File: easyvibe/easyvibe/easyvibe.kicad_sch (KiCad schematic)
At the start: 85 parts, among them SW1 SW_DPDT_x2, U1 TL062, U2 TL062, U3 TL062, U4 TL062

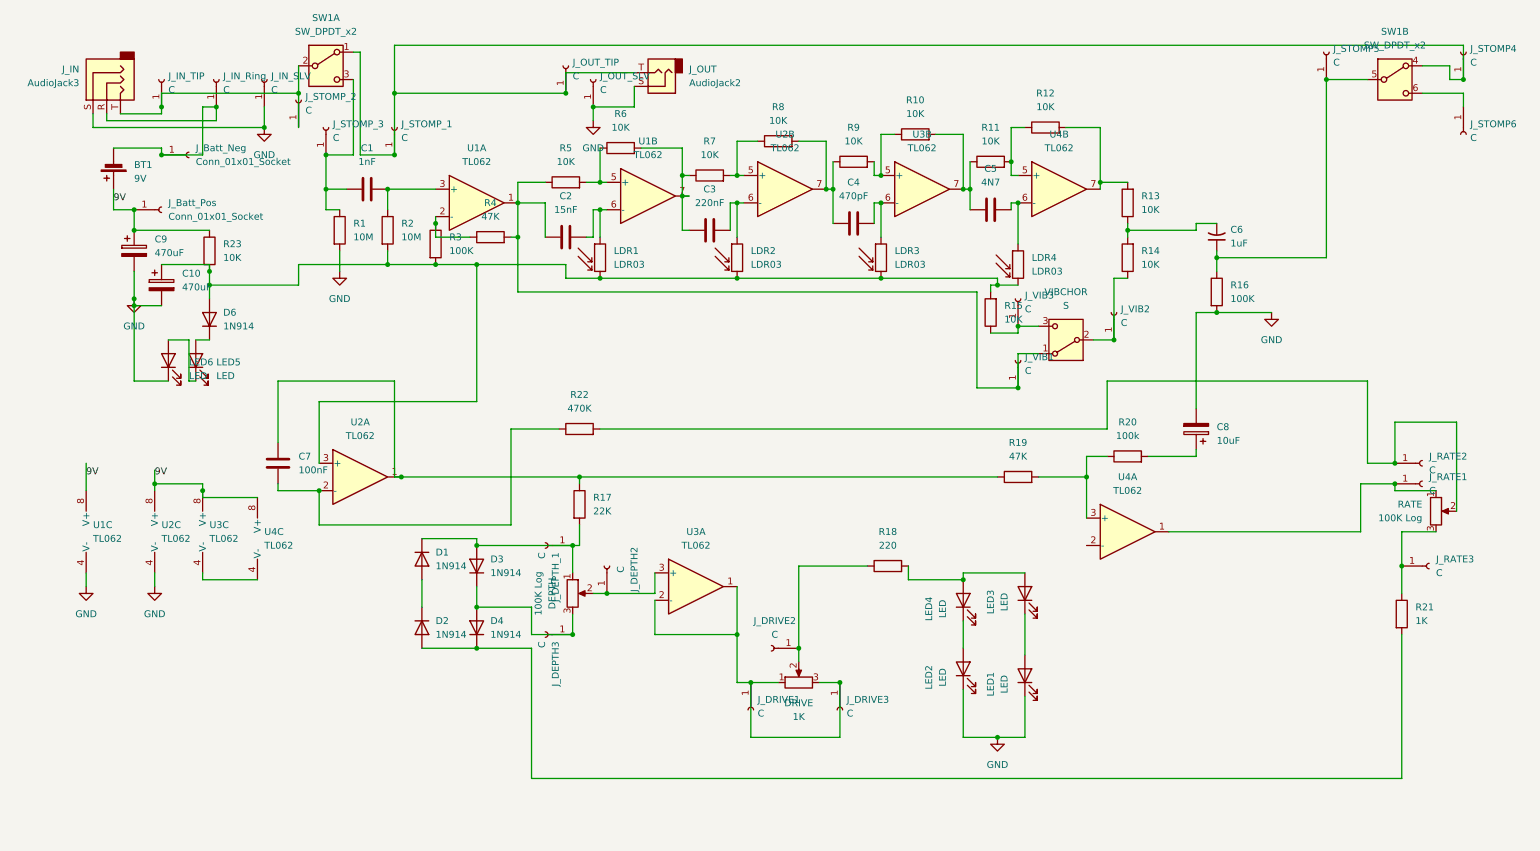
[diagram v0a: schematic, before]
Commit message: got import from digikey models working
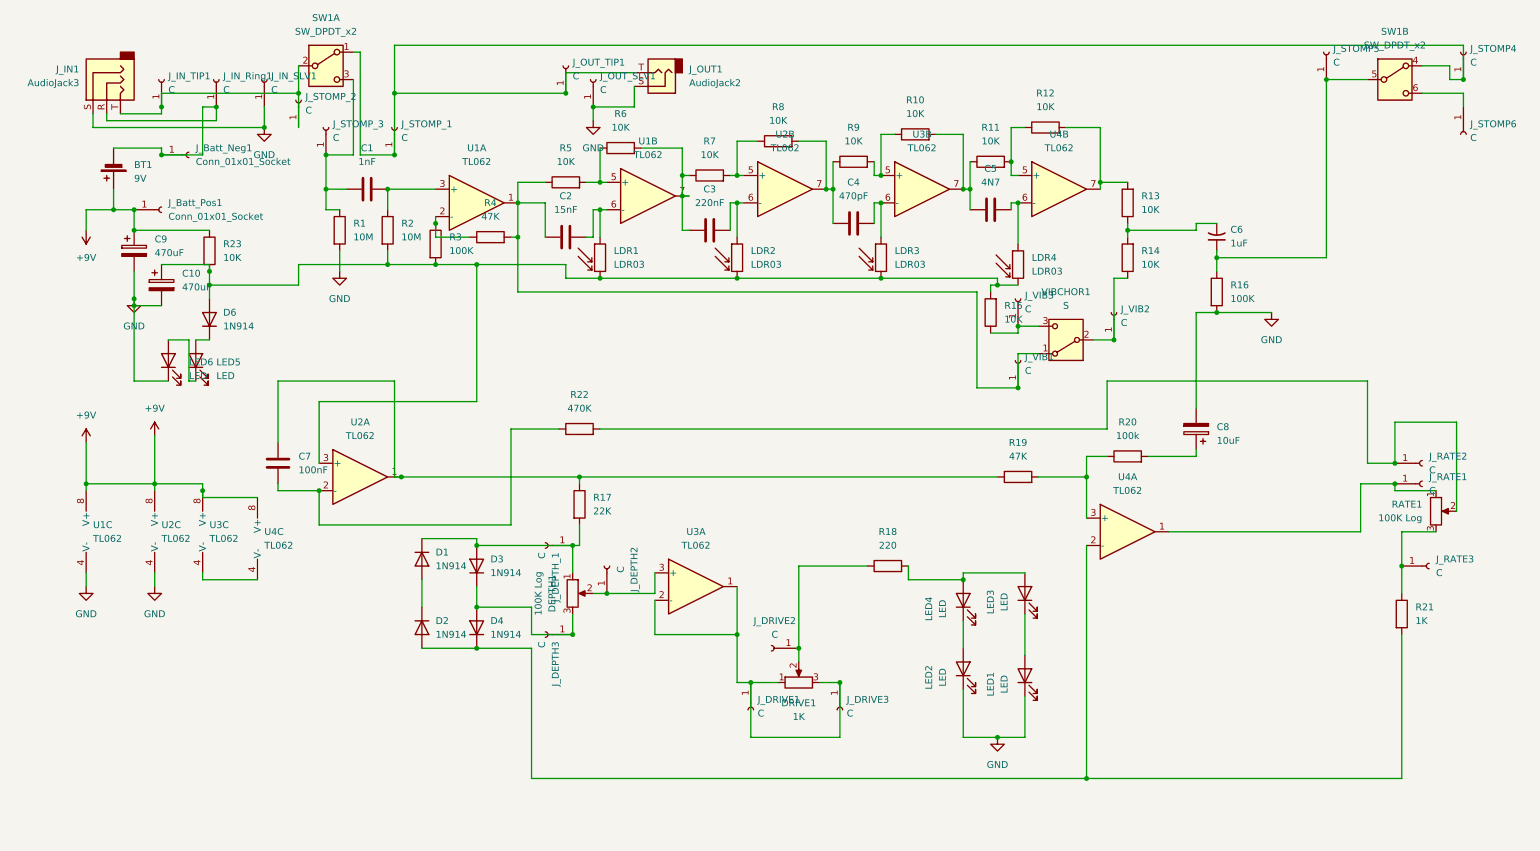
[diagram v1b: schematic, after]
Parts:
- R10, R11, R12, R13, R14, R15, R23, R5, R6, R7, R8, R9: footprint (none) -> Snapeda:YAG_MF25_YAG
- renumbered DEPTH to DEPTH1, DRIVE to DRIVE1, J_Batt_Neg to J_Batt_Neg1, J_Batt_Pos to J_Batt_Pos1, J_IN to J_IN1, J_IN_Ring to J_IN_Ring1, J_IN_SLV to J_IN_SLV1, J_IN_TIP to J_IN_TIP1, J_OUT to J_OUT1, J_OUT_SLV to J_OUT_SLV1, J_OUT_TIP to J_OUT_TIP1, RATE to RATE1, VIBCHOR to VIBCHOR1
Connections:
- net at D2.2 (A), D4.1 (K), R21.2: now also U4.2 (-)
- net 9V renamed +9V

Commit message: all footprints
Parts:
- C1, C2, C3, C5, C7: footprint (none) -> Capacitor_THT:C_Rect_L7.2mm_W2.5mm_P5.00mm_FKS2_FKP2_MKS2_MKP2
- C10, C9: footprint (none) -> Capacitor_THT:CP_Radial_D8.0mm_P3.50mm
- C4: footprint (none) -> Capacitor_THT:C_Rect_L7.2mm_W4.5mm_P5.00mm_FKS2_FKP2_MKS2_MKP2
- C6: footprint (none) -> Capacitor_THT:C_Radial_D5.0mm_H5.0mm_P2.00mm
- C8: footprint (none) -> Capacitor_THT:CP_Radial_D5.0mm_P2.00mm
- D1, D2, D3, D4, D6: footprint (none) -> Snapeda:AFL-W2C8.9D
- DRIVE1: footprint (none) -> Potentiometer_THT:Potentiometer_Runtron_RM-063_Horizontal
- J_Batt_Neg1, J_Batt_Pos1, J_DEPTH2, J_DEPTH3, J_DEPTH_1, J_DRIVE1, J_DRIVE2, J_DRIVE3, J_IN_Ring1, J_IN_SLV1, J_IN_TIP1, J_OUT_SLV1, J_OUT_TIP1, J_RATE1, J_RATE2, J_RATE3, J_STOMP4, J_STOMP5, J_STOMP6, J_STOMP_1, J_STOMP_2, J_STOMP_3, J_VIB1, J_VIB2, J_VIB3: footprint (none) -> Connector_PinSocket_2.54mm:PinSocket_1x01_P2.54mm_Vertical
- LED1, LED2, LED3, LED4, LED5, LED6: footprint (none) -> Snapeda:T-100_4P8X3P15_ONS
- R1, R2: footprint (none) -> Resistor_THT:R_Axial_DIN0207_L6.3mm_D2.5mm_P7.62mm_Horizontal
- R16, R17, R18, R19, R20, R21, R22, R3, R4: footprint (none) -> Snapeda:RES_LR1_TYCO_TYC
- U1, U2, U3, U4: footprint (none) -> Package_DIP:DIP-8_W7.62mm

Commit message: Added board cuts and mounting holes
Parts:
- added H1, H2, H3, H4: MountingHole, MountingHole:MountingHole_3.2mm_M3, symbol Mechanical:MountingHole

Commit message: initial component placement everywheres
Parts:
- removed J_DRIVE1, J_DRIVE2, J_DRIVE3: C, Connector_PinSocket_2.54mm:PinSocket_1x01_P2.54mm_Vertical, symbol Connector:Conn_01x01_Socket
- added R24: 1K, Snapeda:RES_LR1_TYCO_TYC, symbol Device:R
- LDR1, LDR2, LDR3, LDR4: footprint OptoDevice:R_LDR_10x8.5mm_P7.6mm_Vertical -> Snapeda:TO_NSL_19M_ADP
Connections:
- net at DEPTH1.2, J_DEPTH2.1 (Pin_1): now also R24.1; no longer U3.3 (+)
- new net: R24.2, U3.3 (+)

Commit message: some fixes
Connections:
- net at C8.1, R20.2: now also J_RATE1.1 (Pin_1), RATE1.1, U4.1
- net at R7.2, R8.1: now also U2.6 (-); no longer U2.5 (+)
- net at C3.2, LDR2.1: now also U2.5 (+); no longer U2.6 (-)
- net at J_STOMP5.1 (Pin_1), R16.1, SW1.5 (B): now also C6.2; no longer C6.1
- net at R13.1, R14.2: now also C6.1; no longer C6.2
- net at R5.2, R6.1: now also U1.6 (-); no longer U1.5 (+)
- net at C2.2, LDR1.1: now also U1.5 (+); no longer U1.6 (-)
- net at C5.2, LDR4.1: now also U4.5 (+); no longer U4.6 (-)
- net at R10.1, R9.2: now also U3.6 (-); no longer U3.5 (+)
- net at C4.2, LDR3.1: now also U3.5 (+); no longer U3.6 (-)
- net at R11.2, R12.1: now also U4.6 (-); no longer U4.5 (+)
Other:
- moved on the sheet: C6
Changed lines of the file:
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@@
 	)
 	(junction
-		(at 38.1 95.25)
+		(at 179.07 39.37)
 		(diameter 0)
 		(color 0 0 0 0)
 	)
 	(junction
-		(at 189.23 41.91)
+		(at 38.1 95.25)
 		(diameter 0)
 		(color 0 0 0 0)
@@
 	)
 	(junction
-		(at 259.08 90.17)
+		(at 163.83 36.83)
 		(diameter 0)
 		(color 0 0 0 0)
 	)
 	(junction
-		(at 137.16 55.88)
+		(at 259.08 90.17)
 		(diameter 0)
 		(color 0 0 0 0)
 	)
 	(junction
-		(at 189.23 76.2)
+		(at 137.16 55.88)
 		(diameter 0)
 		(color 0 0 0 0)
 	)
 	(junction
-		(at 88.9 105.41)
+		(at 189.23 76.2)
 		(diameter 0)
 		(color 0 0 0 0)
 	)
 	(junction
-		(at 111.76 43.18)
+		(at 88.9 105.41)
 		(diameter 0)
 		(color 0 0 0 0)
@@
 	)
 	(junction
+		(at 137.16 36.83)
+		(diameter 0)
+		(color 0 0 0 0)
+	)
+	(junction
 		(at 88.9 53.34)
 		(diameter 0)
@@
 	)
 	(junction
-		(at 107.95 92.71)
+		(at 218.44 102.87)
 		(diameter 0)
 		(color 0 0 0 0)
 	)
 	(junction
-		(at 163.83 36.83)
+		(at 107.95 92.71)
 		(diameter 0)
 		(color 0 0 0 0)
@@
 	)
 	(junction
-		(at 25.4 60.96)
+		(at 189.23 41.91)
 		(diameter 0)
 		(color 0 0 0 0)
 	)
 	(junction
-		(at 271.78 19.05)
+		(at 25.4 60.96)
 		(diameter 0)
 		(color 0 0 0 0)
 	)
 	(junction
-		(at 179.07 39.37)
+		(at 271.78 19.05)
 		(diameter 0)
 		(color 0 0 0 0)
@@
 	)
 	(junction
+		(at 111.76 43.18)
+		(diameter 0)
+		(color 0 0 0 0)
+	)
+	(junction
 		(at 25.4 46.99)
 		(diameter 0)
@@
 	)
 	(junction
-		(at 204.47 38.1)
+		(at 163.83 41.91)
 		(diameter 0)
 		(color 0 0 0 0)
@@
 	)
 	(junction
-		(at 137.16 41.91)
-		(diameter 0)
-		(color 0 0 0 0)
-	)
-	(junction
 		(at 21.59 43.18)
 		(diameter 0)
@@
 	)
 	(junction
-		(at 163.83 41.91)
+		(at 218.44 88.9)
 		(diameter 0)
 		(color 0 0 0 0)
@@
 	)
 	(junction
-		(at 226.06 62.23)
+		(at 111.76 38.1)
 		(diameter 0)
 		(color 0 0 0 0)
 	)
 	(junction
-		(at 137.16 36.83)
+		(at 226.06 62.23)
 		(diameter 0)
 		(color 0 0 0 0)
@@
 	)
 	(junction
-		(at 201.93 92.71)
+		(at 204.47 38.1)
 		(diameter 0)
 		(color 0 0 0 0)
 	)
 	(junction
-		(at 127 40.64)
+		(at 201.93 92.71)
 		(diameter 0)
 		(color 0 0 0 0)
 	)
 	(junction
-		(at 111.76 38.1)
+		(at 127 40.64)
 		(diameter 0)
 		(color 0 0 0 0)
@@
 	)
 	(junction
+		(at 137.16 41.91)
+		(diameter 0)
+		(color 0 0 0 0)
+	)
+	(junction
 		(at 153.67 39.37)
 		(diameter 0)
@@
 	(wire
 		(pts
-			(xy 217.17 102.87) (xy 252.73 102.87)
+			(xy 217.17 102.87) (xy 218.44 102.87)
 		)
 		(stroke
@@
 	(wire
 		(pts
+			(xy 218.44 102.87) (xy 252.73 102.87)
+		)
+		(stroke
+			(width 0)
+			(type default)
+		)
+	)
+	(wire
+		(pts
 			(xy 266.7 95.25) (xy 259.08 95.25)
 		)
@@
 	(wire
 		(pts
-			(xy 137.16 41.91) (xy 138.43 41.91)
+			(xy 55.88 16.51) (xy 55.88 21.59)
 		)
 		(stroke
@@
 	(wire
 		(pts
-			(xy 55.88 16.51) (xy 55.88 21.59)
+			(xy 270.51 99.06) (xy 270.51 82.55)
 		)
 		(stroke
@@
 	(wire
 		(pts
-			(xy 270.51 99.06) (xy 270.51 82.55)
+			(xy 25.4 74.93) (xy 25.4 60.96)
 		)
 		(stroke
@@
 	(wire
 		(pts
-			(xy 25.4 74.93) (xy 25.4 60.96)
+			(xy 111.76 83.82) (xy 205.74 83.82)
 		)
 		(stroke
@@
 	(wire
 		(pts
-			(xy 111.76 83.82) (xy 205.74 83.82)
+			(xy 119.38 31.75) (xy 127 31.75)
 		)
 		(stroke
@@
 	(wire
 		(pts
-			(xy 119.38 31.75) (xy 127 31.75)
+			(xy 269.24 16.51) (xy 269.24 19.05)
 		)
 		(stroke
@@
 	(wire
 		(pts
-			(xy 269.24 16.51) (xy 269.24 19.05)
+			(xy 88.9 124.46) (xy 99.06 124.46)
 		)
 		(stroke
@@
 	(wire
 		(pts
-			(xy 88.9 124.46) (xy 99.06 124.46)
+			(xy 137.16 36.83) (xy 138.43 36.83)
 		)
 		(stroke
@@
 	(wire
 		(pts
-			(xy 137.16 36.83) (xy 138.43 36.83)
+			(xy 187.96 34.29) (xy 187.96 36.83)
 		)
 		(stroke
@@
 	(wire
 		(pts
-			(xy 187.96 34.29) (xy 187.96 36.83)
+			(xy 218.44 88.9) (xy 213.36 88.9)
 		)
 		(stroke
@@
 	(wire
 		(pts
+			(xy 111.76 38.1) (xy 113.03 38.1)
+		)
+		(stroke
+			(width 0)
+			(type default)
+		)
+	)
+	(wire
+		(pts
 			(xy 189.23 41.91) (xy 189.23 49.53)
 		)
@@
 	(wire
 		(pts
+			(xy 218.44 88.9) (xy 218.44 102.87)
+		)
+		(stroke
+			(width 0)
+			(type default)
+		)
+	)
+	(wire
+		(pts
 			(xy 127 46.99) (xy 128.27 46.99)
 		)
@@
 	(wire
 		(pts
+			(xy 137.16 41.91) (xy 138.43 41.91)
+		)
+		(stroke
+			(width 0)
+			(type default)
+		)
+	)
+	(wire
+		(pts
 			(xy 139.7 140.97) (xy 156.21 140.97)
 		)
@@
 	(wire
 		(pts
-			(xy 111.76 43.18) (xy 113.03 43.18)
-		)
-		(stroke
-			(width 0)
-			(type default)
-		)
-	)
-	(wire
-		(pts
 			(xy 127 36.83) (xy 128.27 36.83)
 		)
@@
 	(wire
 		(pts
-			(xy 222.25 88.9) (xy 213.36 88.9)
+			(xy 222.25 88.9) (xy 218.44 88.9)
 		)
 		(stroke
@@
 	(wire
 		(pts
-			(xy 111.76 38.1) (xy 113.03 38.1)
-		)
-		(stroke
-			(width 0)
-			(type default)
-		)
-	)
-	(wire
-		(pts
 			(xy 111.76 31.75) (xy 111.76 38.1)
 		)
@@
 	(wire
 		(pts
+			(xy 111.76 43.18) (xy 113.03 43.18)
+		)
+		(stroke
+			(width 0)
+			(type default)
+		)
+	)
+	(wire
+		(pts
 			(xy 209.55 38.1) (xy 204.47 38.1)
 		)
@@
 		(lib_id "Amplifier_Operational:TL062")
 		(at 146.05 39.37 0)
+		(mirror x)
 		(unit 2)
 		(body_style 1)
@@
 		(in_pos_files yes)
 		(dnp no)
-		(fields_autoplaced yes)
 		(property "Reference" "U2"
-			(at 146.05 29.21 0)
+			(at 146.05 49.53 0)
 			(show_name no)
 			(do_not_autoplace no)
@@
 		)
 		(property "Value" "TL062"
-			(at 146.05 31.75 0)
+			(at 146.05 46.99 0)
 			(show_name no)
 			(do_not_autoplace no)
@@
 	(symbol
 		(lib_id "Device:C_Small_US")
-		(at 226.06 48.26 180)
+		(at 226.06 48.26 0)
+		(mirror y)
 		(unit 1)
 		(body_style 1)
@@
 		(in_pos_files yes)
 		(dnp no)
-		(fields_autoplaced yes)
 		(property "Reference" "C6"
-			(at 228.6 46.8629 0)
+			(at 228.6 49.6571 0)
 			(show_name no)
 			(do_not_autoplace no)
@@
 		)
 		(property "Value" "1uF"
-			(at 228.6 49.4029 0)
+			(at 228.6 47.1171 0)
 			(show_name no)
 			(do_not_autoplace no)
@@
 		(lib_id "Amplifier_Operational:TL062")
 		(at 120.65 40.64 0)
+		(mirror x)
 		(unit 2)
 		(body_style 1)
@@
 		(in_pos_files yes)
 		(dnp no)
-		(fields_autoplaced yes)
 		(property "Reference" "U1"
-			(at 120.65 30.48 0)
+			(at 120.65 50.8 0)
 			(show_name no)
 			(do_not_autoplace no)
@@
 		)
 		(property "Value" "TL062"
-			(at 120.65 33.02 0)
+			(at 120.65 48.26 0)
 			(show_name no)
 			(do_not_autoplace no)
@@
 		(lib_id "Amplifier_Operational:TL062")
 		(at 171.45 39.37 0)
+		(mirror x)
 		(unit 2)
 		(body_style 1)
@@
 		(in_pos_files yes)
 		(dnp no)
-		(fields_autoplaced yes)
 		(property "Reference" "U3"
-			(at 171.45 29.21 0)
+			(at 171.45 49.53 0)
 			(show_name no)
 			(do_not_autoplace no)
@@
 		)
 		(property "Value" "TL062"
-			(at 171.45 31.75 0)
+			(at 171.45 46.99 0)
 			(show_name no)
 			(do_not_autoplace no)
@@
 		(lib_id "Amplifier_Operational:TL062")
 		(at 196.85 39.37 0)
+		(mirror x)
 		(unit 2)
 		(body_style 1)
@@
 		(in_pos_files yes)
 		(dnp no)
-		(fields_autoplaced yes)
 		(property "Reference" "U4"
-			(at 196.85 29.21 0)
+			(at 196.85 49.53 0)
 			(show_name no)
 			(do_not_autoplace no)
@@
 		)
 		(property "Value" "TL062"
-			(at 196.85 31.75 0)
+			(at 196.85 46.99 0)
 			(show_name no)
 			(do_not_autoplace no)
@@
 		(in_pos_files yes)
 		(dnp no)
-		(fields_autoplaced yes)
 		(property "Reference" "U3"
 			(at 129.54 102.87 0)

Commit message: more tweaks, make board slightly smaller to fit box
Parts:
- removed R24: 1K, Snapeda:RES_LR1_TYCO_TYC, symbol Device:R
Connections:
- net at R21.2, U4.2 (-): now also C10.1, D2.1 (K), D4.2 (A), D6.2 (A), DEPTH1.3, J_DEPTH3.1 (Pin_1), LDR1.2, LDR2.2, LDR3.2, LDR4.2, R15.2, R2.2, R23.2, R3.2, U2.3 (+); no longer D2.2 (A), D4.1 (K)
- net at DEPTH1.1, J_DEPTH_1.1 (Pin_1), R17.2: now also D1.2 (A), D3.1 (K); no longer D1.1 (K), D3.2 (A)
- net at DEPTH1.2, J_DEPTH2.1 (Pin_1): now also U3.3 (+)
- new net: D3.2 (A), D4.1 (K)
- new net: D1.1 (K), D2.2 (A)
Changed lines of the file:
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@@
 	)
 	(junction
-		(at 106.68 121.92)
-		(diameter 0)
-		(color 0 0 0 0)
-	)
-	(junction
 		(at 179.07 111.76)
 		(diameter 0)
@@
 	)
 	(junction
+		(at 59.69 90.17)
+		(diameter 0)
+		(color 0 0 0 0)
+	)
+	(junction
 		(at 111.76 38.1)
 		(diameter 0)
@@
 	)
 	(junction
-		(at 204.47 38.1)
+		(at 78.74 124.46)
 		(diameter 0)
 		(color 0 0 0 0)
 	)
 	(junction
-		(at 201.93 92.71)
+		(at 106.68 121.92)
 		(diameter 0)
 		(color 0 0 0 0)
 	)
 	(junction
-		(at 127 40.64)
+		(at 204.47 38.1)
 		(diameter 0)
 		(color 0 0 0 0)
 	)
 	(junction
-		(at 88.9 116.84)
+		(at 201.93 92.71)
+		(diameter 0)
+		(color 0 0 0 0)
+	)
+	(junction
+		(at 127 40.64)
 		(diameter 0)
 		(color 0 0 0 0)
@@
 	)
 	(junction
+		(at 99.06 124.46)
+		(diameter 0)
+		(color 0 0 0 0)
+	)
+	(junction
 		(at 105.41 21.59)
 		(diameter 0)
@@
 	(wire
 		(pts
-			(xy 99.06 121.92) (xy 106.68 121.92)
-		)
-		(stroke
-			(width 0)
-			(type default)
-		)
-	)
-	(wire
-		(pts
 			(xy 201.93 148.59) (xy 260.35 148.59)
 		)
@@
 	(wire
 		(pts
+			(xy 59.69 90.17) (xy 57.15 90.17)
+		)
+		(stroke
+			(width 0)
+			(type default)
+		)
+	)
+	(wire
+		(pts
 			(xy 25.4 43.18) (xy 25.4 46.99)
 		)
@@
 	(wire
 		(pts
+			(xy 57.15 90.17) (xy 57.15 124.46)
+		)
+		(stroke
+			(width 0)
+			(type default)
+		)
+	)
+	(wire
+		(pts
 			(xy 63.5 50.8) (xy 63.5 54.61)
 		)
@@
 	(wire
 		(pts
+			(xy 106.68 124.46) (xy 99.06 124.46)
+		)
+		(stroke
+			(width 0)
+			(type default)
+		)
+	)
+	(wire
+		(pts
 			(xy 139.7 140.97) (xy 156.21 140.97)
 		)
@@
 	(wire
 		(pts
-			(xy 99.06 116.84) (xy 99.06 121.92)
-		)
-		(stroke
-			(width 0)
-			(type default)
-		)
-	)
-	(wire
-		(pts
 			(xy 16.51 43.18) (xy 16.51 46.99)
 		)
@@
 	(wire
 		(pts
+			(xy 114.3 111.76) (xy 121.92 111.76)
+		)
+		(stroke
+			(width 0)
+			(type default)
+		)
+	)
+	(wire
+		(pts
 			(xy 81.28 44.45) (xy 81.28 45.72)
 		)
@@
 	(wire
 		(pts
+			(xy 57.15 124.46) (xy 78.74 124.46)
+		)
+		(stroke
+			(width 0)
+			(type default)
+		)
+	)
+	(wire
+		(pts
 			(xy 209.55 46.99) (xy 209.55 48.26)
 		)
@@
 	(wire
 		(pts
-			(xy 88.9 116.84) (xy 99.06 116.84)
-		)
-		(stroke
-			(width 0)
-			(type default)
-		)
-	)
-	(wire
-		(pts
 			(xy 259.08 93.98) (xy 259.08 95.25)
 		)
@@
 	(wire
 		(pts
+			(xy 106.68 121.92) (xy 106.68 124.46)
+		)
+		(stroke
+			(width 0)
+			(type default)
+		)
+	)
+	(wire
+		(pts
 			(xy 184.15 66.04) (xy 189.23 66.04)
 		)
@@
 		(lib_id "Device:D")
 		(at 88.9 120.65 90)
+		(mirror x)
 		(unit 1)
 		(body_style 1)
@@
 		(in_pos_files yes)
 		(dnp no)
-		(fields_autoplaced yes)
 		(property "Reference" "D4"
-			(at 91.44 119.3799 90)
+			(at 91.44 121.9201 90)
 			(show_name no)
 			(do_not_autoplace no)
@@
 		)
 		(property "Value" "1N914"
-			(at 91.44 121.9199 90)
+			(at 91.44 119.3801 90)
 			(show_name no)
 			(do_not_autoplace no)
@@
 		(lib_id "Device:D")
 		(at 78.74 107.95 270)
+		(mirror x)
 		(unit 1)
 		(body_style 1)
@@
 		(in_pos_files yes)
 		(dnp no)
-		(fields_autoplaced yes)
 		(property "Reference" "D1"
-			(at 81.28 106.6799 90)
+			(at 81.28 109.2201 90)
 			(show_name no)
 			(do_not_autoplace no)
@@
 		)
 		(property "Value" "1N914"
-			(at 81.28 109.2199 90)
+			(at 81.28 106.6801 90)
 			(show_name no)
 			(do_not_autoplace no)
@@
 	)
 	(symbol
-		(lib_id "Device:R")
-		(at 118.11 111.76 90)
-		(unit 1)
-		(body_style 1)
-		(exclude_from_sim no)
-		(in_bom yes)
-		(on_board yes)
-		(in_pos_files yes)
-		(dnp no)
-		(fields_autoplaced yes)
-		(property "Reference" "R24"
-			(at 118.11 105.41 90)
-			(show_name no)
-			(do_not_autoplace no)
-			(effects
-				(font
-					(size 1.27 1.27)
-				)
-			)
-		)
-		(property "Value" "1K"
-			(at 118.11 107.95 90)
-			(show_name no)
-			(do_not_autoplace no)
-			(effects
-				(font
-					(size 1.27 1.27)
-				)
-			)
-		)
-		(property "Footprint" "Snapeda:RES_LR1_TYCO_TYC"
-			(at 118.11 113.538 90)
-			(hide yes)
-			(show_name no)
-			(do_not_autoplace no)
-			(effects
-				(font
-					(size 1.27 1.27)
-				)
-			)
-		)
-		(property "Datasheet" ""
-			(at 118.11 111.76 0)
-			(hide yes)
-			(show_name no)
-			(do_not_autoplace no)
-			(effects
-				(font
-					(size 1.27 1.27)
-				)
-			)
-		)
-		(property "Description" "Resistor"
-			(at 118.11 111.76 0)
-			(hide yes)
-			(show_name no)
-			(do_not_autoplace no)
-			(effects
-				(font
-					(size 1.27 1.27)
-				)
-			)
-		)
-		(pin "2"
-		)
-		(pin "1"
-		)
-		(instances
-			(project "easyvibe"
-				(path "/4bb4501e-45c8-4c72-91ca-8621e8761900"
-					(reference "R24")
-					(unit 1)
-				)
-			)
-		)
-	)
-	(symbol
 		(lib_id "Connector:Conn_01x01_Socket")
 		(at 110.49 19.05 90)
@@
 		(lib_id "Device:D")
 		(at 78.74 120.65 270)
+		(mirror x)
 		(unit 1)
 		(body_style 1)
@@
 		(in_pos_files yes)
 		(dnp no)
-		(fields_autoplaced yes)
 		(property "Reference" "D2"
-			(at 81.28 119.3799 90)
+			(at 81.28 121.9201 90)
 			(show_name no)
 			(do_not_autoplace no)
@@
 		)
 		(property "Value" "1N914"
-			(at 81.28 121.9199 90)
+			(at 81.28 119.3801 90)
 			(show_name no)
 			(do_not_autoplace no)
@@
 		(lib_id "Device:D")
 		(at 88.9 109.22 90)
+		(mirror x)
 		(unit 1)
 		(body_style 1)
@@
 		(in_pos_files yes)
 		(dnp no)
-		(fields_autoplaced yes)
 		(property "Reference" "D3"
-			(at 91.44 107.9499 90)
+			(at 91.44 110.4901 90)
 			(show_name no)
 			(do_not_autoplace no)
@@
 		)
 		(property "Value" "1N914"
-			(at 91.44 110.4899 90)
+			(at 91.44 107.9501 90)
 			(show_name no)
 			(do_not_autoplace no)
